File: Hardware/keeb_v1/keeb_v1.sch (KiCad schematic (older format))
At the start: 25 parts, among them J1 USB_mini_micro_B, K1 KEYSW, K2 KEYSW, K3 KEYSW, K4 KEYSW, SW1 SW_Push, U1 ATMEGA32U4, X1 XTAL_GND

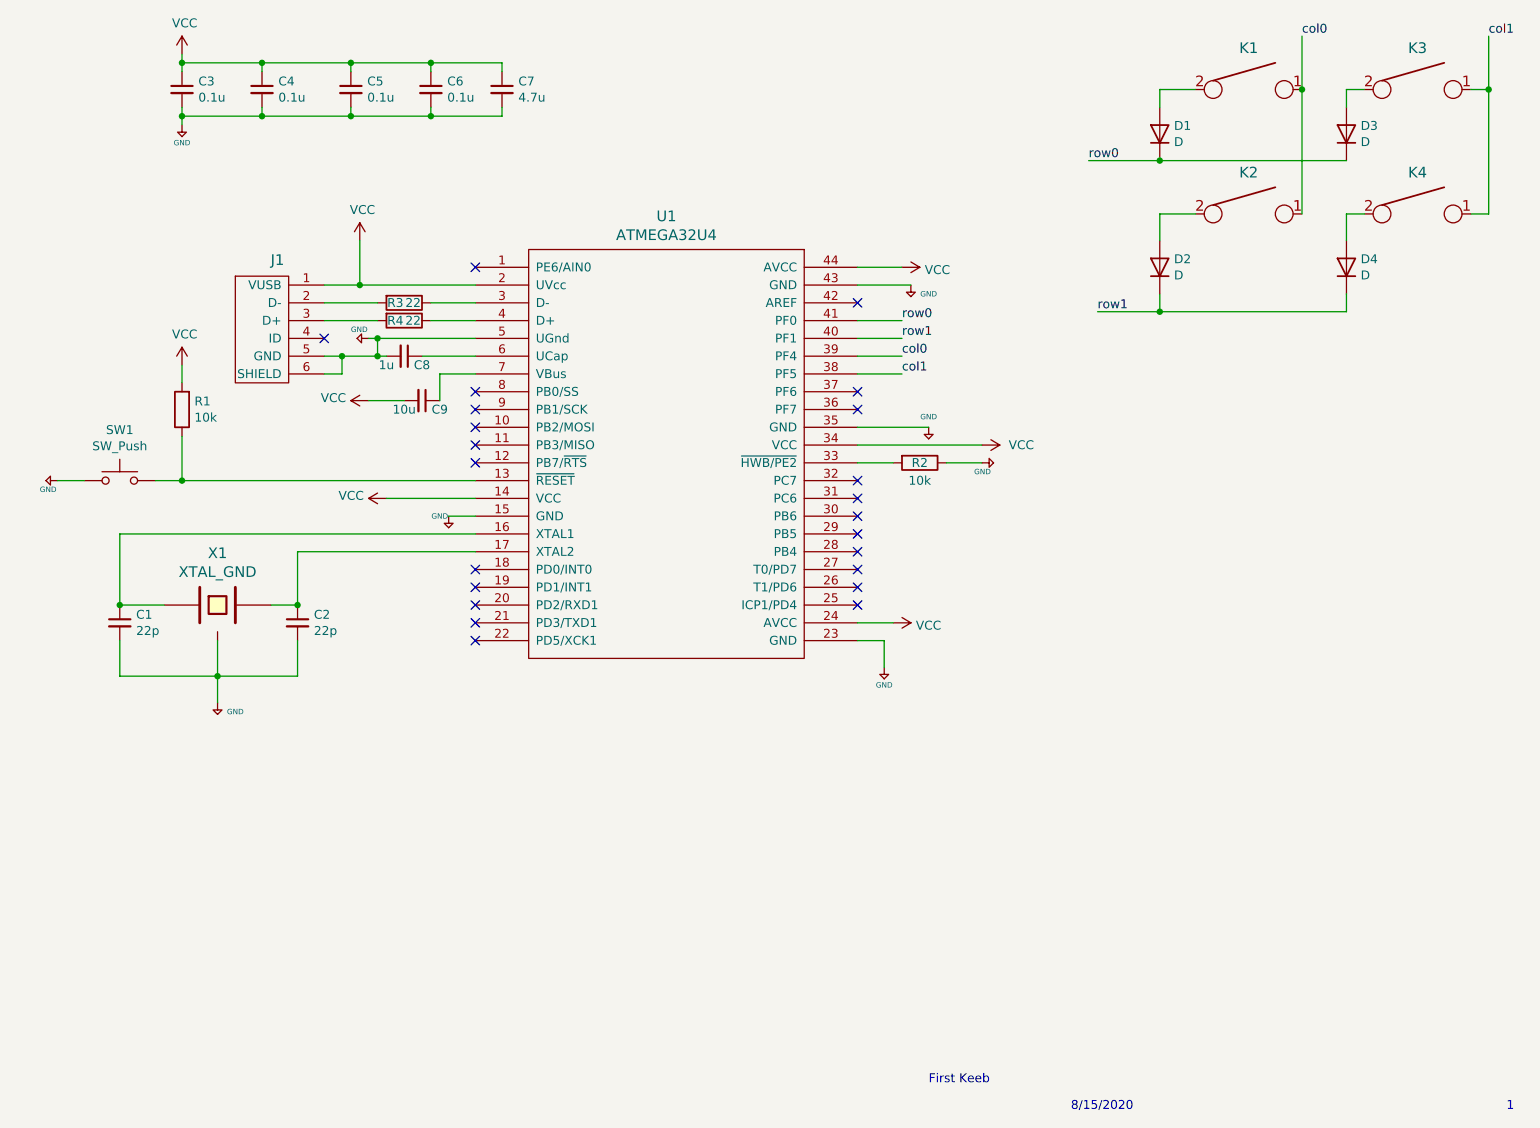
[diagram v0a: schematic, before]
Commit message: Started routing. Need to go back and check lengths and also add mounting holes
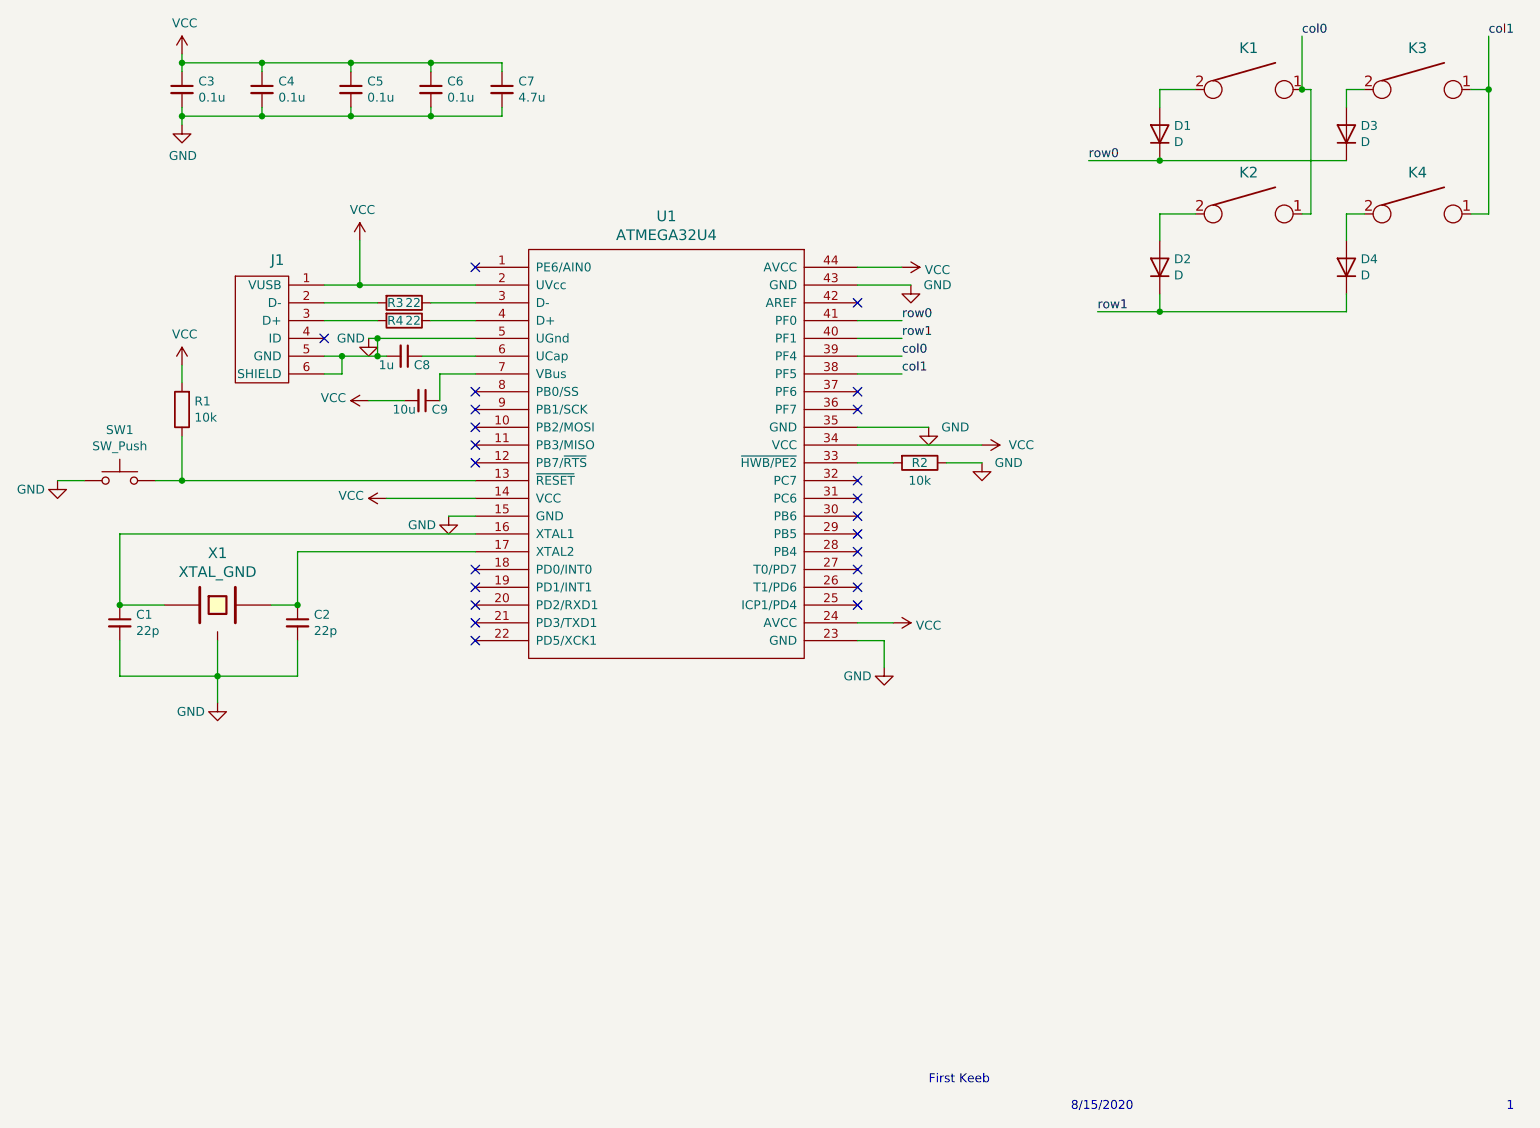
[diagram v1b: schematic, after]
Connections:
- net +5V renamed GND
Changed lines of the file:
@@
 	3800 5200 3800 5000
 Connection ~ 3350 5200
-$Comp
-L keyboard_parts:GND #PWR0101
-U 1 1 5F38E79C
-P 3350 5350
-F 0 "#PWR0101" H 3350 5400 20  0001 C CNN
-F 1 "GND" H 3450 5300 30  0000 C CNN
-F 2 "" H 3350 5350 60  0000 C CNN
-F 3 "" H 3350 5350 60  0000 C CNN
-	1    3350 5350
-	1    0    0    -1
-$EndComp
 Wire Wire Line
 	3350 5200 3350 5350
@@
 F 3 "" H 3150 1700 50  0001 C CNN
 	1    3150 1700
-	1    0    0    -1
-$EndComp
-$Comp
-L keyboard_parts:GND #PWR0103
-U 1 1 5F39C342
-P 3150 2100
-F 0 "#PWR0103" H 3150 2150 20  0001 C CNN
-F 1 "GND" H 3150 2000 30  0000 C CNN
-F 2 "" H 3150 2100 60  0000 C CNN
-F 3 "" H 3150 2100 60  0000 C CNN
-	1    3150 2100
 	1    0    0    -1
 $EndComp
@@
 	1    0    0    -1
 $EndComp
-$Comp
-L keyboard_parts:GND #PWR0105
-U 1 1 5F3B54EB
-P 2450 4100
-F 0 "#PWR0105" H 2450 4150 20  0001 C CNN
-F 1 "GND" V 2500 4000 30  0000 L CNN
-F 2 "" H 2450 4100 60  0000 C CNN
-F 3 "" H 2450 4100 60  0000 C CNN
-	1    2450 4100
-	0    1    1    0
-$EndComp
 Wire Wire Line
 	2450 4100 2600 4100
@@
 	3000 4100 3150 4100
 Connection ~ 3150 4100
-$Comp
-L keyboard_parts:GND #PWR0106
-U 1 1 5F3B7C98
-P 7650 4000
-F 0 "#PWR0106" H 7650 4050 20  0001 C CNN
-F 1 "GND" V 7600 3950 30  0000 L CNN
-F 2 "" H 7650 4000 60  0000 C CNN
-F 3 "" H 7650 4000 60  0000 C CNN
-	1    7650 4000
-	0    -1   -1   0
-$EndComp
 $Comp
 L Device:R R2
@@
 Wire Wire Line
 	4250 3400 4300 3400
-$Comp
-L keyboard_parts:GND #PWR0108
-U 1 1 5F3D1941
-P 4200 3300
-F 0 "#PWR0108" H 4200 3350 20  0001 C CNN
-F 1 "GND" V 4150 3200 30  0000 L CNN
-F 2 "" H 4200 3300 60  0000 C CNN
-F 3 "" H 4200 3300 60  0000 C CNN
-	1    4200 3300
-	0    1    1    0
-$EndComp
 Wire Wire Line
 	4200 3300 4250 3300
@@
 	0    1    1    0
 $EndComp
-$Comp
-L keyboard_parts:GND #PWR0113
-U 1 1 5F3DC20F
-P 7100 5150
-F 0 "#PWR0113" H 7100 5200 20  0001 C CNN
-F 1 "GND" H 7100 5050 30  0000 C CNN
-F 2 "" H 7100 5150 60  0000 C CNN
-F 3 "" H 7100 5150 60  0000 C CNN
-	1    7100 5150
-	1    0    0    -1
-$EndComp
 Wire Wire Line
 	6950 2900 7200 2900
@@
 Wire Wire Line
 	4600 3500 4800 3500
-$Comp
-L keyboard_parts:GND #PWR0115
-U 1 1 5F3E6379
-P 4650 4300
-F 0 "#PWR0115" H 4650 4350 20  0001 C CNN
-F 1 "GND" H 4600 4300 30  0000 C CNN
-F 2 "" H 4650 4300 60  0000 C CNN
-F 3 "" H 4650 4300 60  0000 C CNN
-	1    4650 4300
-	1    0    0    -1
-$EndComp
 Wire Wire Line
 	4650 4300 4800 4300
-$Comp
-L keyboard_parts:GND #PWR0116
-U 1 1 5F3E9299
-P 7350 3800
-F 0 "#PWR0116" H 7350 3850 20  0001 C CNN
-F 1 "GND" H 7350 3859 30  0000 C CNN
-F 2 "" H 7350 3800 60  0000 C CNN
-F 3 "" H 7350 3800 60  0000 C CNN
-	1    7350 3800
-	1    0    0    -1
-$EndComp
 Wire Wire Line
 	6950 3800 7350 3800
 Wire Wire Line
 	6950 3900 7650 3900
-$Comp
-L keyboard_parts:GND #PWR0117
-U 1 1 5F3EEA1A
-P 7250 3000
-F 0 "#PWR0117" H 7250 3050 20  0001 C CNN
-F 1 "GND" H 7350 2950 30  0000 C CNN
-F 2 "" H 7250 3000 60  0000 C CNN
-F 3 "" H 7250 3000 60  0000 C CNN
-	1    7250 3000
-	1    0    0    -1
-$EndComp
 Wire Wire Line
 	6950 3000 7250 3000
@@
 $EndComp
 Wire Wire Line
-	8850 1900 8650 1900
-Wire Wire Line
 	8650 1900 8650 2000
 Wire Wire Line
@@
 	9700 1900 9800 1900
 Wire Wire Line
-	9450 1900 9450 2600
-Wire Wire Line
 	8850 2600 8650 2600
 Wire Wire Line
@@
 	9700 3150 9700 3050
 Wire Wire Line
-	9700 2750 9700 2600
-Wire Wire Line
-	9700 2600 9800 2600
-Wire Wire Line
 	10400 2600 10500 2600
-Wire Wire Line
-	10500 2600 10500 1900
 Wire Wire Line
 	10500 1900 10400 1900
@@
 Wire Wire Line
 	9450 1600 9450 1900
-Connection ~ 9450 1900
 Wire Wire Line
 	10500 1900 10500 1600
-Connection ~ 10500 1900
 Text Label 7200 3200 0    50   ~ 0
 row0
@@
 	4550 3200 4800 3200
 NoConn ~ 3950 3300
+Wire Wire Line
+	9450 2600 9500 2600
+Wire Wire Line
+	9500 2600 9500 1900
+Wire Wire Line
+	9500 1900 9450 1900
+Connection ~ 9450 1900
+Wire Wire Line
+	9800 2600 9700 2600
+Wire Wire Line
+	9700 2600 9700 2750
+Wire Wire Line
+	10500 2600 10500 1900
+Connection ~ 10500 1900
+Wire Wire Line
+	8650 1900 8850 1900
+$Comp
+L power:GND #PWR?
+U 1 1 5F38AD9B
+P 3150 2100
+F 0 "#PWR?" H 3150 1850 50  0001 C CNN
+F 1 "GND" H 3155 1927 50  0000 C CNN
+F 2 "" H 3150 2100 50  0001 C CNN
+F 3 "" H 3150 2100 50  0001 C CNN
+	1    3150 2100
+	1    0    0    -1
+$EndComp
+$Comp
+L power:GND #PWR?
+U 1 1 5F38E72B
+P 4650 4300
+F 0 "#PWR?" H 4650 4050 50  0001 C CNN
+F 1 "GND" H 4500 4250 50  0000 C CNN
+F 2 "" H 4650 4300 50  0001 C CNN
+F 3 "" H 4650 4300 50  0001 C CNN
+	1    4650 4300
+	1    0    0    -1
+$EndComp
+$Comp
+L power:GND #PWR?
+U 1 1 5F390710
+P 7100 5150
+F 0 "#PWR?" H 7100 4900 50  0001 C CNN
+F 1 "GND" H 6950 5100 50  0000 C CNN
+F 2 "" H 7100 5150 50  0001 C CNN
+F 3 "" H 7100 5150 50  0001 C CNN
+	1    7100 5150
+	1    0    0    -1
+$EndComp
+$Comp
+L power:GND #PWR?
+U 1 1 5F39196B
+P 7350 3800
+F 0 "#PWR?" H 7350 3550 50  0001 C CNN
+F 1 "GND" H 7500 3800 50  0000 C CNN
+F 2 "" H 7350 3800 50  0001 C CNN
+F 3 "" H 7350 3800 50  0001 C CNN
+	1    7350 3800
+	1    0    0    -1
+$EndComp
+$Comp
+L power:GND #PWR?
+U 1 1 5F392DD5
+P 7250 3000
+F 0 "#PWR?" H 7250 2750 50  0001 C CNN
+F 1 "GND" H 7400 3000 50  0000 C CNN
+F 2 "" H 7250 3000 50  0001 C CNN
+F 3 "" H 7250 3000 50  0001 C CNN
+	1    7250 3000
+	1    0    0    -1
+$EndComp
+$Comp
+L power:GND #PWR?
+U 1 1 5F393A8C
+P 7650 4000
+F 0 "#PWR?" H 7650 3750 50  0001 C CNN
+F 1 "GND" H 7800 4000 50  0000 C CNN
+F 2 "" H 7650 4000 50  0001 C CNN
+F 3 "" H 7650 4000 50  0001 C CNN
+	1    7650 4000
+	1    0    0    -1
+$EndComp
+$Comp
+L power:GND #PWR?
+U 1 1 5F3946A1
+P 3350 5350
+F 0 "#PWR?" H 3350 5100 50  0001 C CNN
+F 1 "GND" H 3200 5300 50  0000 C CNN
+F 2 "" H 3350 5350 50  0001 C CNN
+F 3 "" H 3350 5350 50  0001 C CNN
+	1    3350 5350
+	1    0    0    -1
+$EndComp
+$Comp
+L power:GND #PWR?
+U 1 1 5F394F8D
+P 4200 3300
+F 0 "#PWR?" H 4200 3050 50  0001 C CNN
+F 1 "GND" H 4100 3300 50  0000 C CNN
+F 2 "" H 4200 3300 50  0001 C CNN
+F 3 "" H 4200 3300 50  0001 C CNN
+	1    4200 3300
+	1    0    0    -1
+$EndComp
+$Comp
+L power:GND #PWR?
+U 1 1 5F395B82
+P 2450 4100
+F 0 "#PWR?" H 2450 3850 50  0001 C CNN
+F 1 "GND" H 2300 4050 50  0000 C CNN
+F 2 "" H 2450 4100 50  0001 C CNN
+F 3 "" H 2450 4100 50  0001 C CNN
+	1    2450 4100
+	1    0    0    -1
+$EndComp
 $EndSCHEMATC
